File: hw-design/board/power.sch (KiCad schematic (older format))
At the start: 21 parts, among them Q1 2N7002, Q2 2N7002, Q3 FDN306P, U1 NCP1117DT50G, U2 NCP1117DT33G

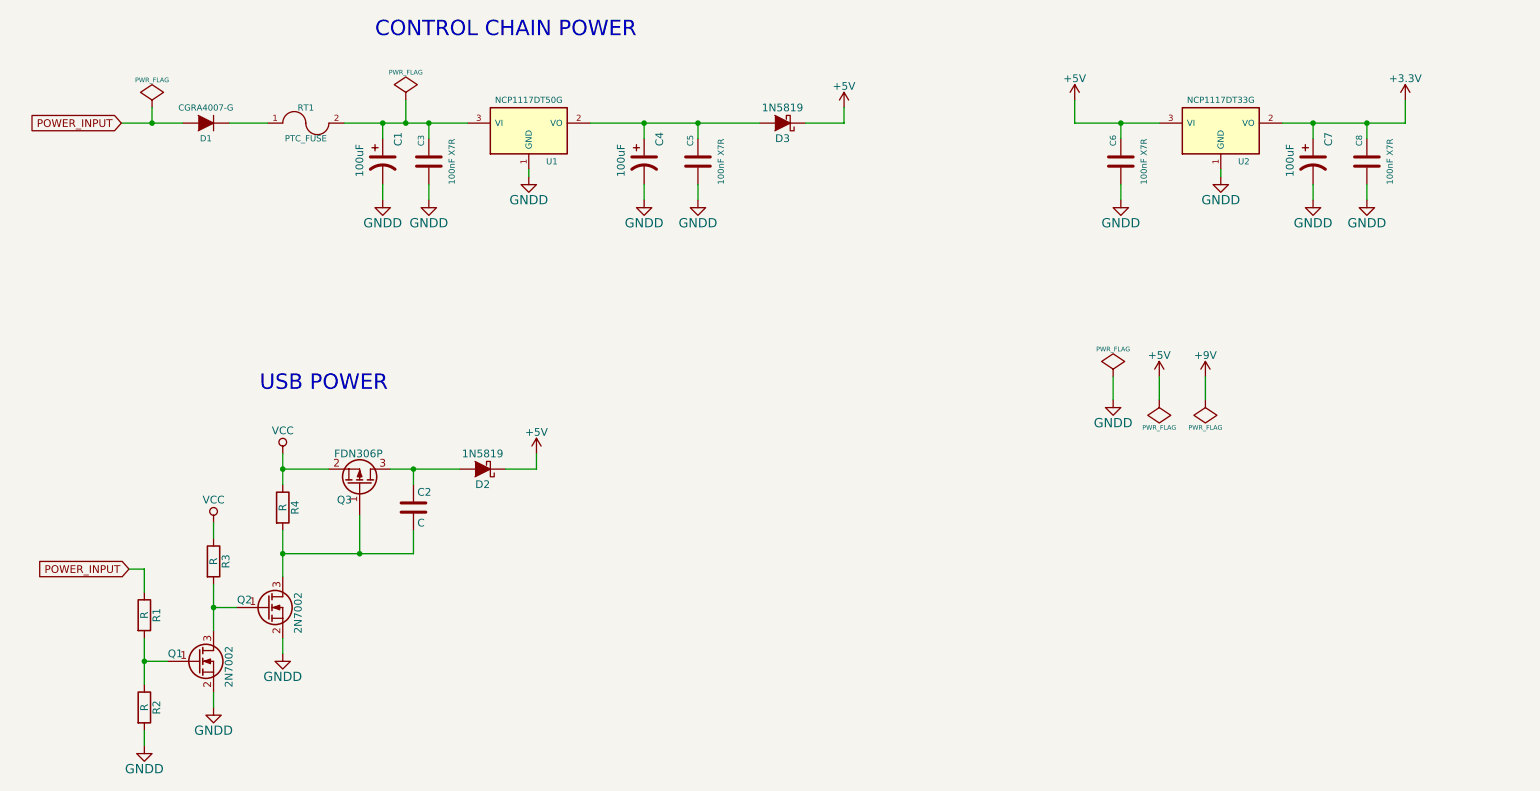
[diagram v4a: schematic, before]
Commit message: sch: adding values and MPN to components
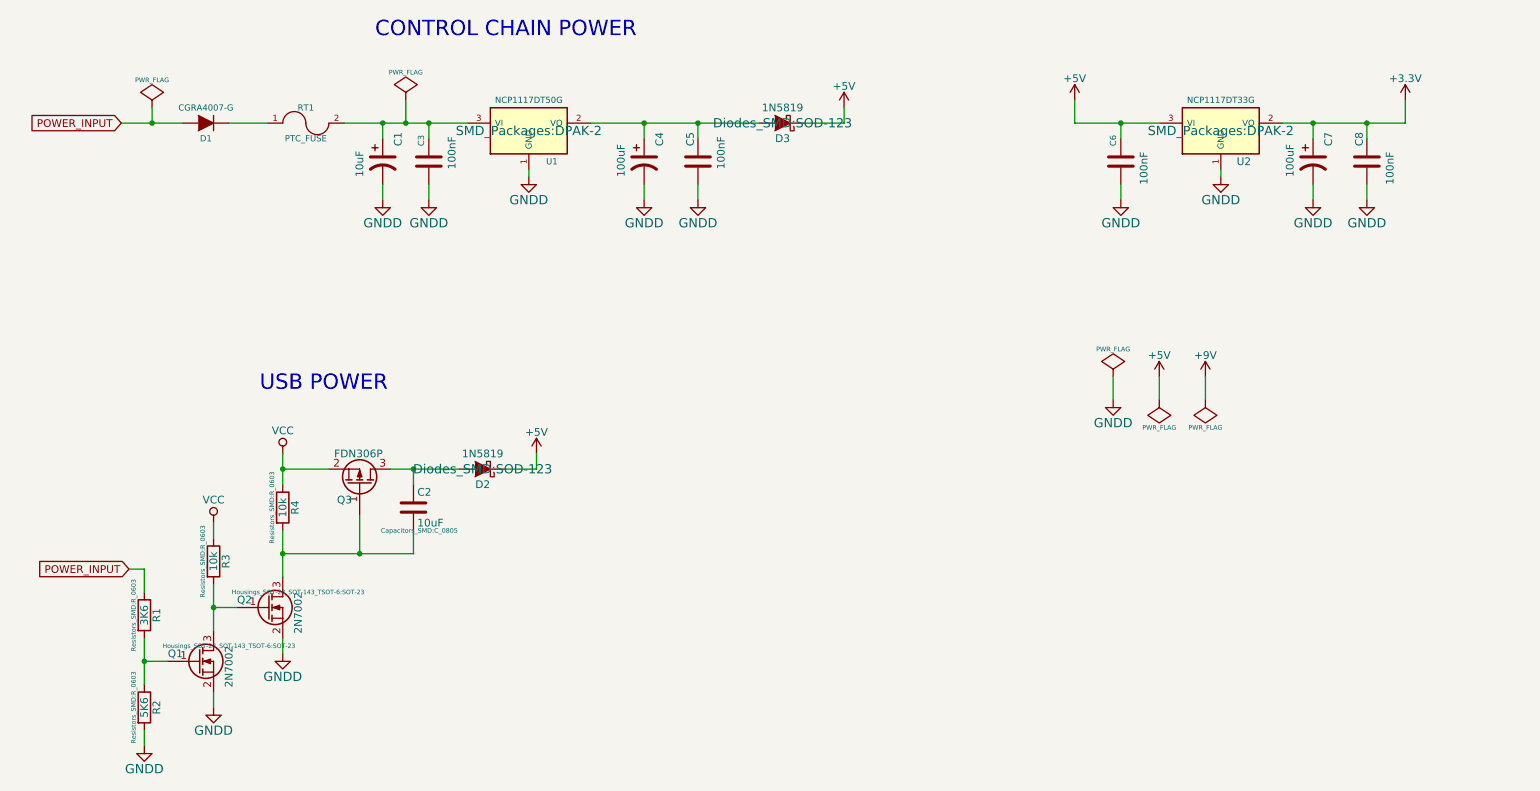
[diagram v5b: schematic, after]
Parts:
- C1: value 100uF -> 10uF; MPN (none) -> UWX1E100MCL1GB
- C2: value C -> 10uF; footprint (none) -> Capacitors_SMD:C_0805; MPN (none) -> GRM219R61E106KA12D
- C3, C5, C6, C8: value 100nF X7R -> 100nF; MPN (none) -> C1608X7R1E104K080AA
- C4, C7: MPN (none) -> UWX1C101MCL1GB
- D1: MPN (none) -> CGRA4007-G
- D2, D3: footprint (none) -> Diodes_SMD:SOD-123; MPN (none) -> 1N5819HW-7-F
- Q1, Q2: footprint (none) -> Housings_SOT-23_SOT-143_TSOT-6:SOT-23; MPN (none) -> 2N7002P,215
- Q3: MPN (none) -> FDN306P_F095
- R1: value R -> 3K6; footprint (none) -> Resistors_SMD:R_0603; MPN (none) -> RMCF0603JT3K60
- R2: value R -> 5K6; footprint (none) -> Resistors_SMD:R_0603; MPN (none) -> RMCF0603JT5K60
- R3, R4: value R -> 10k; footprint (none) -> Resistors_SMD:R_0603; MPN (none) -> RMCF0603JT10K0
- RT1: MPN (none) -> 0ZCB0050FF2G
- U1: footprint (none) -> SMD_Packages:DPAK-2; MPN (none) -> NCP1117DT50G
- U2: footprint (none) -> SMD_Packages:DPAK-2; MPN (none) -> NCP1117DT33G

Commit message: sch: setting footprints and updating BOM
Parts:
- C1: footprint Capacitors_ThroughHole:Capacitor5x6RM2.5 -> Capacitors_SMD:c_elec_5x5.3
- C4, C7: footprint Capacitors_ThroughHole:Capacitor5x6RM2.5 -> Capacitors_SMD:c_elec_6.3x5.3
- Q3: footprint (none) -> local-footprints:SOT-23-fairchild
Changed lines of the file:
@@
 F 0 "C7" V 9300 1950 50  0000 L CNN
 F 1 "100uF" V 9050 1750 50  0000 L CNN
-F 2 "Capacitors_ThroughHole:Capacitor5x6RM2.5" H 9200 1850 60  0001 C CNN
+F 2 "Capacitors_SMD:c_elec_6.3x5.3" H 9200 1850 60  0001 C CNN
 F 3 "~" H 9200 1850 60  0000 C CNN
 F 4 "UWX1C101MCL1GB" H 0   0   50  0001 C CNN "MPN"
@@
 F 0 "C4" V 4950 1950 50  0000 L CNN
 F 1 "100uF" V 4700 1750 50  0000 L CNN
-F 2 "Capacitors_ThroughHole:Capacitor5x6RM2.5" H 4850 1850 60  0001 C CNN
+F 2 "Capacitors_SMD:c_elec_6.3x5.3" H 4850 1850 60  0001 C CNN
 F 3 "~" H 4850 1850 60  0000 C CNN
 F 4 "UWX1C101MCL1GB" H 0   0   50  0001 C CNN "MPN"
@@
 F 0 "C1" V 3250 1950 50  0000 L CNN
 F 1 "10uF" V 3000 1750 50  0000 L CNN
-F 2 "Capacitors_ThroughHole:Capacitor5x6RM2.5" H 3150 1850 60  0001 C CNN
+F 2 "Capacitors_SMD:c_elec_5x5.3" H 3150 1850 60  0001 C CNN
 F 3 "~" H 3150 1850 60  0000 C CNN
 F 4 "UWX1E100MCL1GB" H 0   0   50  0001 C CNN "MPN"
@@
 F 0 "Q3" V 2900 3900 50  0000 R CNN
 F 1 "FDN306P" V 3200 4100 50  0000 R CNN
-F 2 "" H 3200 4050 29  0000 C CNN
+F 2 "local-footprints:SOT-23-fairchild" H 3200 4050 29  0000 C CNN
 F 3 "" H 3000 3950 60  0000 C CNN
 F 4 "FDN306P_F095" H 0   0   50  0001 C CNN "MPN"
